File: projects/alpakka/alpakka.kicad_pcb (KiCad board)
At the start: 2 copper layers, 130 x 51 mm, 85 parts, among them P1 Conn_01x20_Pin, P2 Conn_01x20_Pin, P3 Headers 4P IN, P4 Blade, P6 Conn_01x02, U1 Alpsalpine_RKJXV, U10 ST_LSM6, U12 ST_LSM6, U2 Alpsalpine_RKJXV, U3 Alpsalpine_EC10E, U6 NXP_PCAL6416A, U8 NXP_PCAL6416A

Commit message: Updated hardware generation detection
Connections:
- U6 pad 7: unconnected-(U6-P6-Pad7) -> /A6
- U6 pad 8: unconnected-(U6-P7-Pad8) -> /A7
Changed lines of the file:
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@@
 	(net 43 "/A2")
 	(net 44 "unconnected-(U6-P5-Pad6)")
-	(net 45 "unconnected-(U6-P6-Pad7)")
-	(net 46 "unconnected-(U6-P7-Pad8)")
+	(net 45 "/A7")
+	(net 46 "/A6")
 	(net 47 "Net-(D2-K)")
 	(net 48 "Net-(D3-K)")
@@
 			(size 0.28 0.8)
 			(layers "F.Cu" "F.Paste" "F.Mask")
-			(net 45 "unconnected-(U6-P6-Pad7)")
+			(net 46 "/A6")
 			(pinfunction "P6")
-			(pintype "input+no_connect")
+			(pintype "input")
 			(clearance 0.127)
 			(zone_connect 2)
@@
 			(size 0.28 0.8)
 			(layers "F.Cu" "F.Paste" "F.Mask")
-			(net 46 "unconnected-(U6-P7-Pad8)")
+			(net 45 "/A7")
 			(pinfunction "P7")
-			(pintype "input+no_connect")
+			(pintype "input")
 			(clearance 0.127)
 			(zone_connect 2)

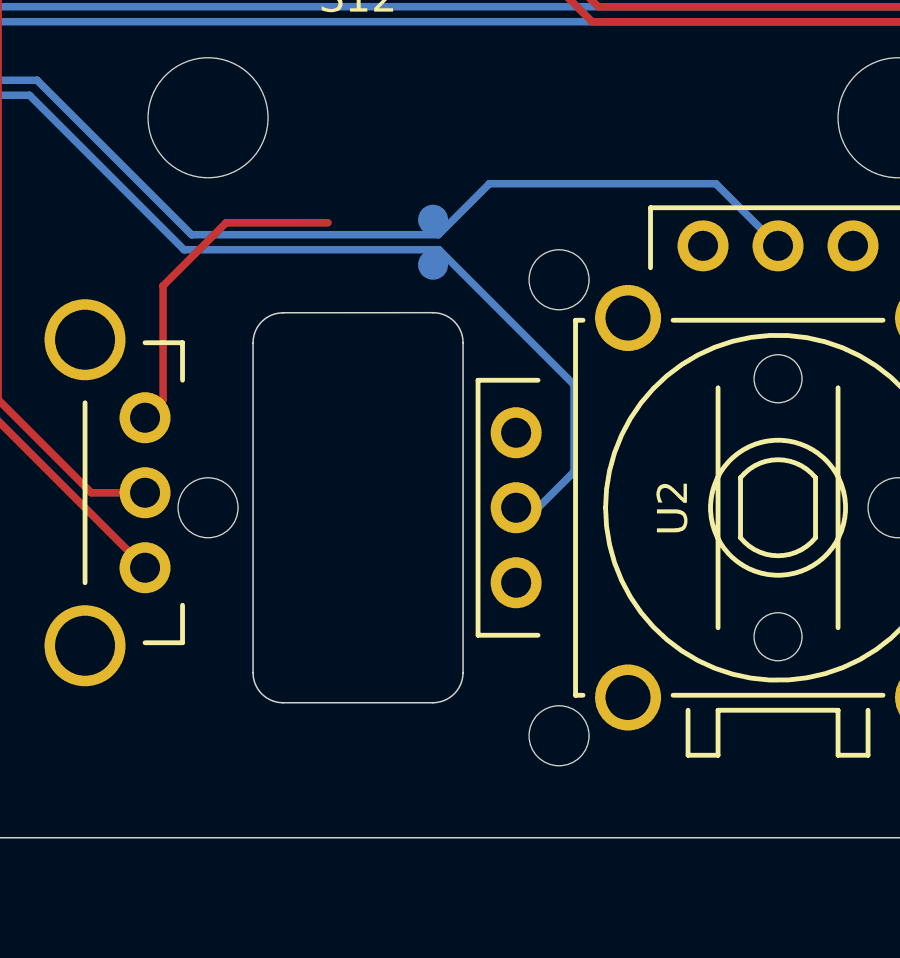
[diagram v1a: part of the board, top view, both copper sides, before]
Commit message: Adjusted scrollwheel support holes position
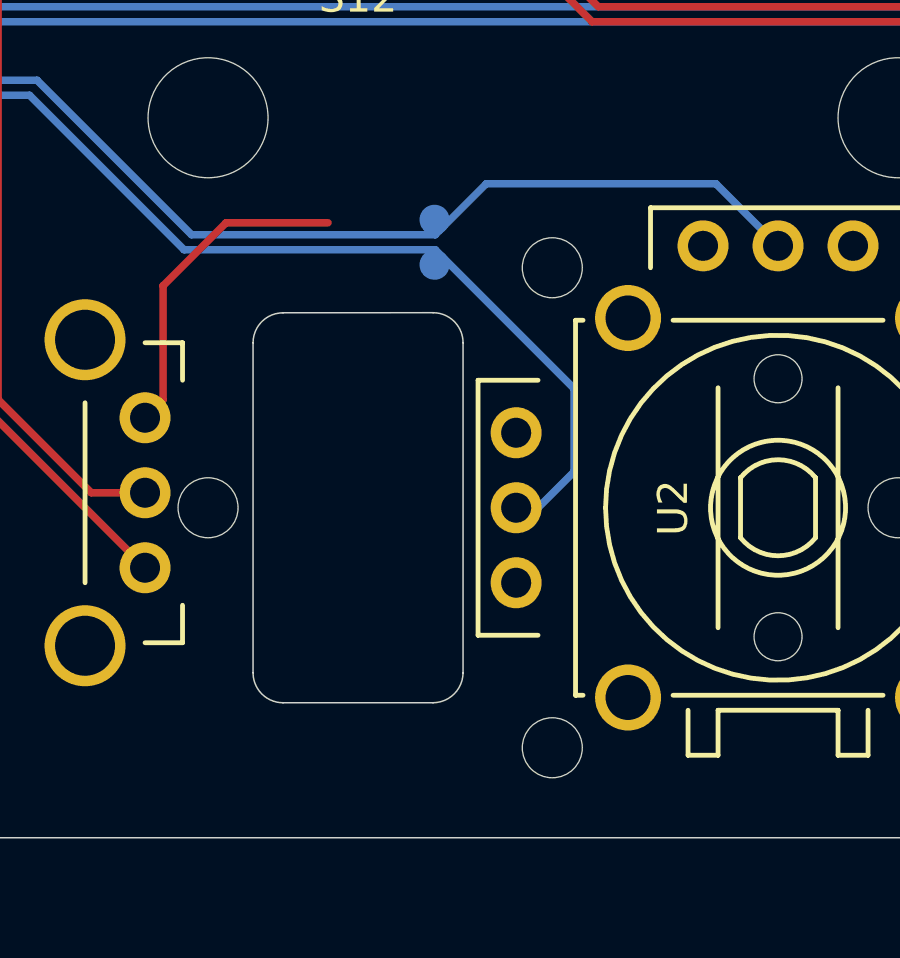
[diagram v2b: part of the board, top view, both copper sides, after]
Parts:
- moved REF** 0.46 mm to (126.5, 83.0)
- moved REF** 0.46 mm to (126.5, 67.0)
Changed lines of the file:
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@@
 	(footprint "ILO_fp:NPTH_2mm"
 		(layer "F.Cu")
-		(at 126.7 82.6)
+		(at 126.475 83)
 		(descr "Mounting Hole 4mm, no annular")
 		(tags "mounting hole 4mm no annular")
@@
 	(footprint "ILO_fp:NPTH_2mm"
 		(layer "F.Cu")
-		(at 126.7 67.4)
+		(at 126.475 67)
 		(descr "Mounting Hole 4mm, no annular")
 		(tags "mounting hole 4mm no annular")
@@
 	(footprint "ILO_fp:Pad_1mm"
 		(layer "B.Cu")
-		(at 122.5 65.4 180)
+		(at 122.55 65.4 180)
 		(property "Reference" "TPA1"
 			(at 1 0 0)
@@
 	(footprint "ILO_fp:Pad_1mm"
 		(layer "B.Cu")
-		(at 122.5 66.9 180)
+		(at 122.55 66.9 180)
 		(property "Reference" "TPA0"
 			(at 1 0 0)
@@
 	)
 	(segment
-		(start 114.45 65.9)
-		(end 122.675 65.9)
+		(start 131.929993 64.2)
+		(end 133.999991 66.269998)
 		(width 0.25)
 		(layer "B.Cu")
@@
 	)
 	(segment
-		(start 124.375 64.2)
-		(end 131.929993 64.2)
+		(start 122.575 65.9)
+		(end 124.275 64.2)
 		(width 0.25)
 		(layer "B.Cu")
@@
 	)
 	(segment
-		(start 98.75 62.9)
-		(end 100.9 60.75)
+		(start 124.275 64.2)
+		(end 131.929993 64.2)
 		(width 0.25)
 		(layer "B.Cu")
@@
 	)
 	(segment
-		(start 98.75 65)
-		(end 98.75 62.9)
+		(start 114.45 65.9)
+		(end 122.575 65.9)
 		(width 0.25)
 		(layer "B.Cu")
@@
 	)
 	(segment
-		(start 122.675 65.9)
-		(end 124.375 64.2)
+		(start 109.3 60.75)
+		(end 114.45 65.9)
 		(width 0.25)
 		(layer "B.Cu")
@@
 	)
 	(segment
-		(start 109.3 60.75)
-		(end 114.45 65.9)
+		(start 98.75 65)
+		(end 98.75 62.9)
 		(width 0.25)
 		(layer "B.Cu")
@@
 	)
 	(segment
-		(start 131.929993 64.2)
-		(end 133.999991 66.269998)
+		(start 98.75 62.9)
+		(end 100.9 60.75)
 		(width 0.25)
 		(layer "B.Cu")
@@
 	)
 	(segment
-		(start 122.7 66.4)
-		(end 114.2 66.4)
+		(start 99.25 63.113755)
+		(end 99.25 65)
 		(width 0.25)
 		(layer "B.Cu")
@@
 	)
 	(segment
-		(start 101.113755 61.25)
-		(end 99.25 63.113755)
+		(start 127.2 73.8)
+		(end 127.2 71.025)
 		(width 0.25)
 		(layer "B.Cu")
@@
 	)
 	(segment
-		(start 127.2 73.8)
-		(end 127.2 70.9)
+		(start 122.575 66.4)
+		(end 114.2 66.4)
 		(width 0.25)
 		(layer "B.Cu")
@@
 	)
 	(segment
-		(start 114.2 66.4)
-		(end 109.05 61.25)
+		(start 127.2 71.025)
+		(end 122.575 66.4)
 		(width 0.25)
 		(layer "B.Cu")
@@
 	)
 	(segment
-		(start 127.2 70.9)
-		(end 122.7 66.4)
+		(start 125.999991 75.000009)
+		(end 127.2 73.8)
 		(width 0.25)
 		(layer "B.Cu")
@@
 	)
 	(segment
-		(start 109.05 61.25)
-		(end 101.113755 61.25)
+		(start 125.269998 75.000009)
+		(end 125.999991 75.000009)
 		(width 0.25)
 		(layer "B.Cu")
@@
 	)
 	(segment
-		(start 125.269998 75.000009)
-		(end 125.999991 75.000009)
+		(start 114.2 66.4)
+		(end 109.05 61.25)
 		(width 0.25)
 		(layer "B.Cu")
@@
 	)
 	(segment
-		(start 125.999991 75.000009)
-		(end 127.2 73.8)
+		(start 109.05 61.25)
+		(end 101.113755 61.25)
 		(width 0.25)
 		(layer "B.Cu")
@@
 	)
 	(segment
-		(start 99.25 63.113755)
-		(end 99.25 65)
+		(start 101.113755 61.25)
+		(end 99.25 63.113755)
 		(width 0.25)
 		(layer "B.Cu")

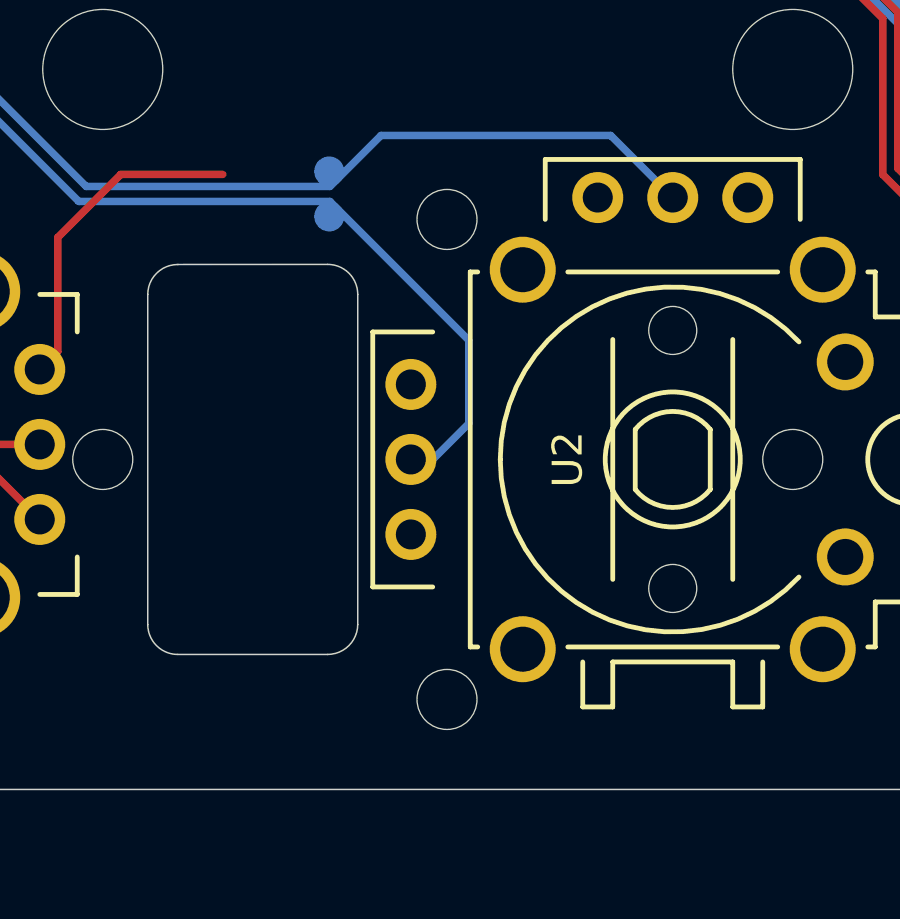
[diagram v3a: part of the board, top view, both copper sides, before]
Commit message: Readjusted scroll holder holes
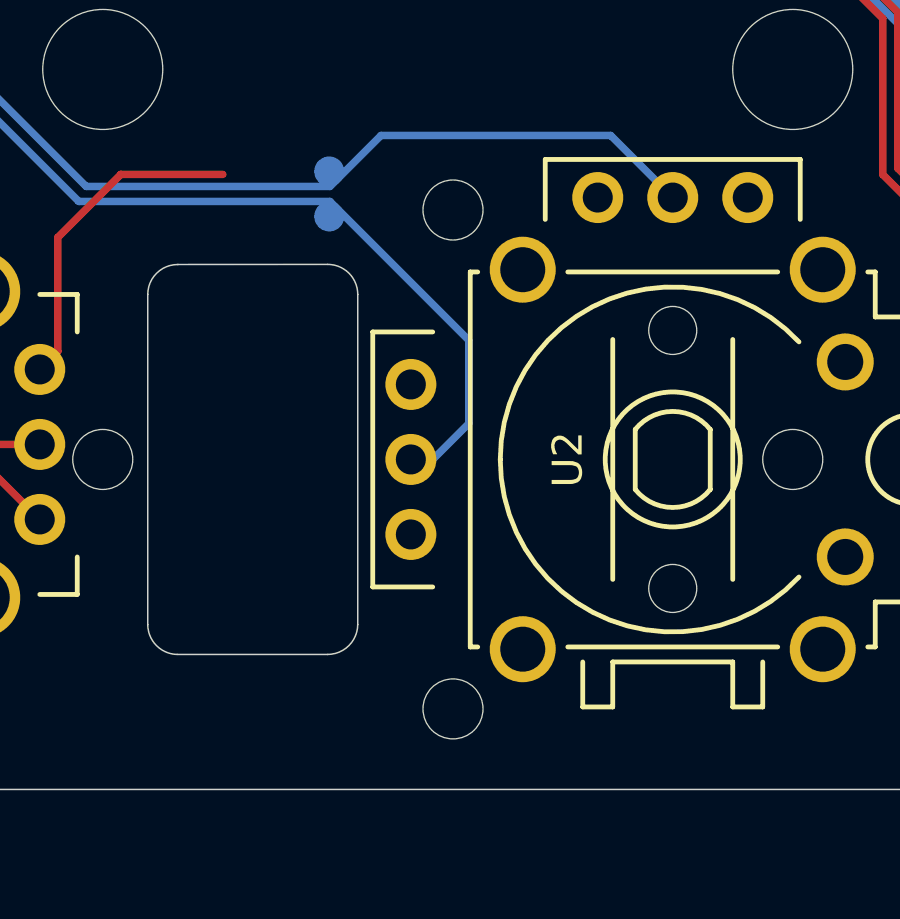
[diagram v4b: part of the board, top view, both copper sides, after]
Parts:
- moved REF** 0.37 mm to (126.7, 83.3)
- moved REF** 0.37 mm to (126.7, 66.7)
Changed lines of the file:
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@@
 	(footprint "ILO_fp:NPTH_2mm"
 		(layer "F.Cu")
-		(at 126.475 83)
+		(at 126.675 83.315)
 		(descr "Mounting Hole 4mm, no annular")
 		(tags "mounting hole 4mm no annular")
@@
 	(footprint "ILO_fp:NPTH_2mm"
 		(layer "F.Cu")
-		(at 126.475 67)
+		(at 126.675 66.685)
 		(descr "Mounting Hole 4mm, no annular")
 		(tags "mounting hole 4mm no annular")

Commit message: Fixed export script rotation in bottom layer, Fixed L1R1 switch origin
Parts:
- moved S15 1.27 mm to (61.5, 43.8)
- moved S16 1.27 mm to (138.5, 43.8)
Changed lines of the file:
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@@
 			(at 0 -7 0)
 			(layer "F.Fab")
+			(hide yes)
 			(effects
 				(font
@@
 			(at 0 -7 180)
 			(layer "F.Fab")
+			(hide yes)
 			(effects
 				(font
@@
 			(at 0 -7 0)
 			(layer "F.Fab")
+			(hide yes)
 			(effects
 				(font
@@
 			(at 0 -7 180)
 			(layer "F.Fab")
+			(hide yes)
 			(effects
 				(font
@@
 			(at 0 -7 180)
 			(layer "F.Fab")
+			(hide yes)
 			(effects
 				(font
@@
 			(at 0 -7 0)
 			(layer "F.Fab")
+			(hide yes)
 			(effects
 				(font
@@
 			(at 0 -6.999999 0)
 			(layer "F.Fab")
+			(hide yes)
 			(effects
 				(font
@@
 			(at 0 -7 -90)
 			(layer "F.Fab")
+			(hide yes)
 			(effects
 				(font
@@
 			(at 0 -7 0)
 			(layer "F.Fab")
+			(hide yes)
 			(effects
 				(font
@@
 			(at 0 -7 90)
 			(layer "F.Fab")
+			(hide yes)
 			(effects
 				(font
@@
 			(at 0 -7 -90)
 			(layer "F.Fab")
+			(hide yes)
 			(effects
 				(font
@@
 			(at 0 -6.999999 0)
 			(layer "F.Fab")
+			(hide yes)
 			(effects
 				(font
@@
 			(at 0 -7 0)
 			(layer "F.Fab")
+			(hide yes)
 			(effects
 				(font
@@
 	(footprint "ILO_fp:Alpsalpine_SKHHL"
 		(layer "F.Cu")
-		(at 61.5 42.5 180)
+		(at 61.5 43.77 180)
 		(property "Reference" "S15"
-			(at 0 -3.75 180)
+			(at 0 -2.48 180)
 			(layer "F.SilkS")
 			(effects
@@
 			(at 0 -5.5 180)
 			(layer "F.Fab")
+			(hide yes)
 			(effects
 				(font
@@
 		(attr through_hole)
 		(fp_line
-			(start 3.75 2.5)
-			(end 3.75 -1.25)
+			(start 3.75 3.77)
+			(end 3.75 0.02)
 			(stroke
 				(width 0.16)
@@
 		)
 		(fp_line
-			(start 3.75 -3.75)
-			(end 3.75 -4.25)
+			(start 3.75 -2.48)
+			(end 3.75 -2.98)
 			(stroke
 				(width 0.16)
@@
 		)
 		(fp_line
-			(start 1.75 3.5)
-			(end 1.75 2.5)
+			(start 1.75 4.77)
+			(end 1.75 3.77)
 			(stroke
 				(width 0.16)
@@
 		)
 		(fp_line
-			(start -1.75 3.5)
-			(end 1.75 3.5)
+			(start -1.75 4.77)
+			(end 1.75 4.77)
 			(stroke
 				(width 0.16)
@@
 		)
 		(fp_line
-			(start -1.75 2.5)
-			(end -1.75 3.5)
+			(start -1.75 3.77)
+			(end -1.75 4.77)
 			(stroke
 				(width 0.16)
@@
 		)
 		(fp_line
-			(start -2.25 -1.5)
-			(end 2.25 -1.5)
+			(start -2.25 -0.23)
+			(end 2.25 -0.23)
 			(stroke
 				(width 0.16)
@@
 		)
 		(fp_line
-			(start -3.75 2.5)
-			(end 3.75 2.5)
+			(start -3.75 3.77)
+			(end 3.75 3.77)
 			(stroke
 				(width 0.16)
@@
 		)
 		(fp_line
-			(start -3.75 2.5)
-			(end -3.75 -1.25)
+			(start -3.75 3.77)
+			(end -3.75 0.02)
 			(stroke
 				(width 0.16)
@@
 		)
 		(fp_line
-			(start -3.75 -3.75)
-			(end -3.75 -4.25)
+			(start -3.75 -2.48)
+			(end -3.75 -2.98)
 			(stroke
 				(width 0.16)
@@
 		)
 		(pad "" thru_hole circle
-			(at -3.5 -2.5 180)
+			(at -3.5 -1.23 180)
 			(size 2 2)
 			(drill 1.3)
@@
 		)
 		(pad "" thru_hole circle
-			(at 3.5 -2.5 180)
+			(at 3.5 -1.23 180)
 			(size 2 2)
 			(drill 1.3)
@@
 		)
 		(pad "1" thru_hole circle
-			(at 2.25 0 180)
+			(at 2.25 1.27 180)
 			(size 1.7 1.7)
 			(drill 1)
@@
 		)
 		(pad "2" thru_hole circle
-			(at -2.25 0 180)
+			(at -2.25 1.27 180)
 			(size 1.7 1.7)
 			(drill 1)
@@
 		(model "${KIPRJMOD}/../../symbols/step/SKHHLM.step"
 			(offset
-				(xyz 0 -0.5 0)
+				(xyz 0 -1.77 0)
 			)
 			(scale
@@
 	(footprint "ILO_fp:Alpsalpine_SKHHL"
 		(layer "F.Cu")
-		(at 138.5 42.5 180)
+		(at 138.5 43.77 180)
 		(property "Reference" "S16"
-			(at 0 -3.75 180)
+			(at 0 -2.48 180)
 			(layer "F.SilkS")
 			(effects
@@
 			(at 0 -5.5 180)
 			(layer "F.Fab")
+			(hide yes)
 			(effects
 				(font
@@
 		(attr through_hole)
 		(fp_line
-			(start 3.75 2.5)
-			(end 3.75 -1.25)
+			(start 3.75 3.77)
+			(end 3.75 0.02)
 			(stroke
 				(width 0.16)
@@
 		)
 		(fp_line
-			(start 3.75 -3.75)
-			(end 3.75 -4.25)
+			(start 3.75 -2.48)
+			(end 3.75 -2.98)
 			(stroke
 				(width 0.16)
@@
 		)
 		(fp_line
-			(start 1.75 3.5)
-			(end 1.75 2.5)
+			(start 1.75 4.77)
+			(end 1.75 3.77)
 			(stroke
 				(width 0.16)
@@
 		)
 		(fp_line
-			(start -1.75 3.5)
-			(end 1.75 3.5)
+			(start -1.75 4.77)
+			(end 1.75 4.77)
 			(stroke
 				(width 0.16)
@@
 		)
 		(fp_line
-			(start -1.75 2.5)
-			(end -1.75 3.5)
+			(start -1.75 3.77)
+			(end -1.75 4.77)
 			(stroke
 				(width 0.16)
@@
 		)
 		(fp_line
-			(start -2.25 -1.5)
-			(end 2.25 -1.5)
+			(start -2.25 -0.23)
+			(end 2.25 -0.23)
 			(stroke
 				(width 0.16)
@@
 		)
 		(fp_line
-			(start -3.75 2.5)
-			(end 3.75 2.5)
+			(start -3.75 3.77)
+			(end 3.75 3.77)
 			(stroke
 				(width 0.16)
@@
 		)
 		(fp_line
-			(start -3.75 2.5)
-			(end -3.75 -1.25)
+			(start -3.75 3.77)
+			(end -3.75 0.02)
 			(stroke
 				(width 0.16)
@@
 		)
 		(fp_line
-			(start -3.75 -3.75)
-			(end -3.75 -4.25)
+			(start -3.75 -2.48)
+			(end -3.75 -2.98)
 			(stroke
 				(width 0.16)
@@
 		)
 		(pad "" thru_hole circle
-			(at -3.5 -2.5 180)
+			(at -3.5 -1.23 180)
 			(size 2 2)
 			(drill 1.3)
@@
 		)
 		(pad "" thru_hole circle
-			(at 3.5 -2.5 180)
+			(at 3.5 -1.23 180)
 			(size 2 2)
 			(drill 1.3)
@@
 		)
 		(pad "1" thru_hole circle
-			(at 2.25 0 180)
+			(at 2.25 1.27 180)
 			(size 1.7 1.7)
 			(drill 1)
@@
 		)
 		(pad "2" thru_hole circle
-			(at -2.25 0 180)
+			(at -2.25 1.27 180)
 			(size 1.7 1.7)
 			(drill 1)
@@
 		(model "${KIPRJMOD}/../../symbols/step/SKHHLM.step"
 			(offset
-				(xyz 0 -0.5 0)
+				(xyz 0 -1.77 0)
 			)
 			(scale

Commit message: Shifted GPIO nets on the bottom row of the top connector
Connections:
- D1 pad 2: /GP9 -> /GP10
- D2 pad 2: /GP8 -> /GP9
- D3 pad 2: /GP7 -> /GP8
- D4 pad 2: /GP6 -> /GP7
- P1 pad 13: /GP6 -> /GP7
- P1 pad 14: /GP7 -> /GP8
- P1 pad 15: /GP8 -> /GP9
- P1 pad 16: /GP9 -> /GP10
- P1 pad 17: /GP10 -> /GP11
- P1 pad 18: /GP11 -> /GP12
- P1 pad 19: /GP12 -> /GP13
- P1 pad 20: /GP13 -> /GP14
- P4 pad 1: /GP12 -> /GP13
- R5 pad 1: /GP13 -> /GP14
- R5 pad 2: /GP12 -> /GP13
- R6 pad 2: /GP12 -> /GP13
- R7 pad 1: /GP13 -> /GP14
- TPS0 pad 1: /GP10 -> /GP11
- TPS1 pad 1: /GP11 -> /GP12
- U3 pad 1: /GP10 -> /GP11
- U3 pad 2: /GP11 -> /GP12
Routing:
- net /GP13: track 13.6 -> 61.2 mm, vias 1 -> 3
- net /GP12: track 61.2 -> 34.5 mm, vias 3 -> 1
- net /GP10: track 35.8 -> 9.24 mm
- net /GP14: track 0.00 -> 13.6 mm, vias 0 -> 1
- net /GP6: track 9.04 -> 0.00 mm, vias 1 -> 0
- net /GP7: track 11.5 -> 9.04 mm
- net /GP9: track 9.24 -> 11.4 mm
- net /GP11: track 34.5 -> 35.8 mm

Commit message: Alpakka added touch ref path, Reordered debug pins, Swapped analog 2-3, Removed wheel support holes, Added silkscreen
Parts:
- removed R7: DNP, ILO_fp:0603_compact
- removed the REF** at (126.7, 83.3)
- removed the REF** at (126.7, 66.7)
- P3: value Headers 4P IN -> Conn_01x04
- moved TPA2 1.50 mm to (82.8, 65.4)
- moved TPA3 1.49 mm to (82.8, 66.9)
- moved TPP0 1.00 mm to (109.5, 45.0)
- moved TPP1 1.00 mm to (109.5, 46.5)
- moved TPS0 1.00 mm to (109.5, 54.5)
- moved TPS1 1.00 mm to (109.5, 53.0)
- moved R6 0.99 mm to (110.5, 55.9), turned to 0 degrees
- moved R5 0.99 mm to (110.5, 54.5), turned to 0 degrees
- renumbered R6 to R5, R5 to R6
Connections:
- P1 pad 3: unconnected-(P1-Pin_3-Pad3) -> /GP4
- P3 pad 1: /UART0_TX -> /GND
- P3 pad 2: /UART0_RX -> /RUN
- P3 pad 3: /GND -> /UART0_RX
- P3 pad 4: /RUN -> /UART0_TX
- R5 pad 1: Net-(R6-Pad1) -> /GP14
- R5 pad 2: /GP13 -> /GP4
- R6 pad 1: /GP14 -> /GP13
- R6 pad 2: /GP13 -> /GP4
- U1 pad 2: /ADC3 -> /ADC2
- U1 pad 5: /ADC2 -> /ADC3
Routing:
- net /GP4: track 0.00 -> 23.5 mm, vias 0 -> 1
- net /RUN: track 30.6 -> 44.5 mm
- net /ADC2: track 48.6 -> 39.4 mm
- net /ADC3: track 42.0 -> 47.5 mm, vias 2 -> 0
- net /UART0_TX: track 12.3 -> 7.57 mm
- net Net-(R6-Pad1): track 2.32 -> 0.00 mm
- net /GP13: track 61.2 -> 62.7 mm
- net /GP11: track 35.8 -> 36.8 mm
- net /GP12: track 34.5 -> 35.5 mm
- net /UART0_RX: track 7.81 -> 7.12 mm
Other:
- board text added: "A0"
- board text added: "A1"
- board text added: "A2"
- board text added: "A3"
- board text added: "Alpakka b1.0.0"
- board text added: "RESET"
- board text added: "RX"
- board text added: "S0"
- board text added: "S1"
- board text added: "TX"
- board text removed: "Alpakka"
- board text removed: "DNF"
- board text removed: "b1.0.0-beta1"
